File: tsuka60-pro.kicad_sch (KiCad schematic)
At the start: 173 parts, among them J1 USB_C_Receptacle_USB2.0, J2 Conn_01x04_MountingPin, SW1 SW_Reset, U1 ATmega32U4-M, U2 SRV05-4, Y1 16MHz

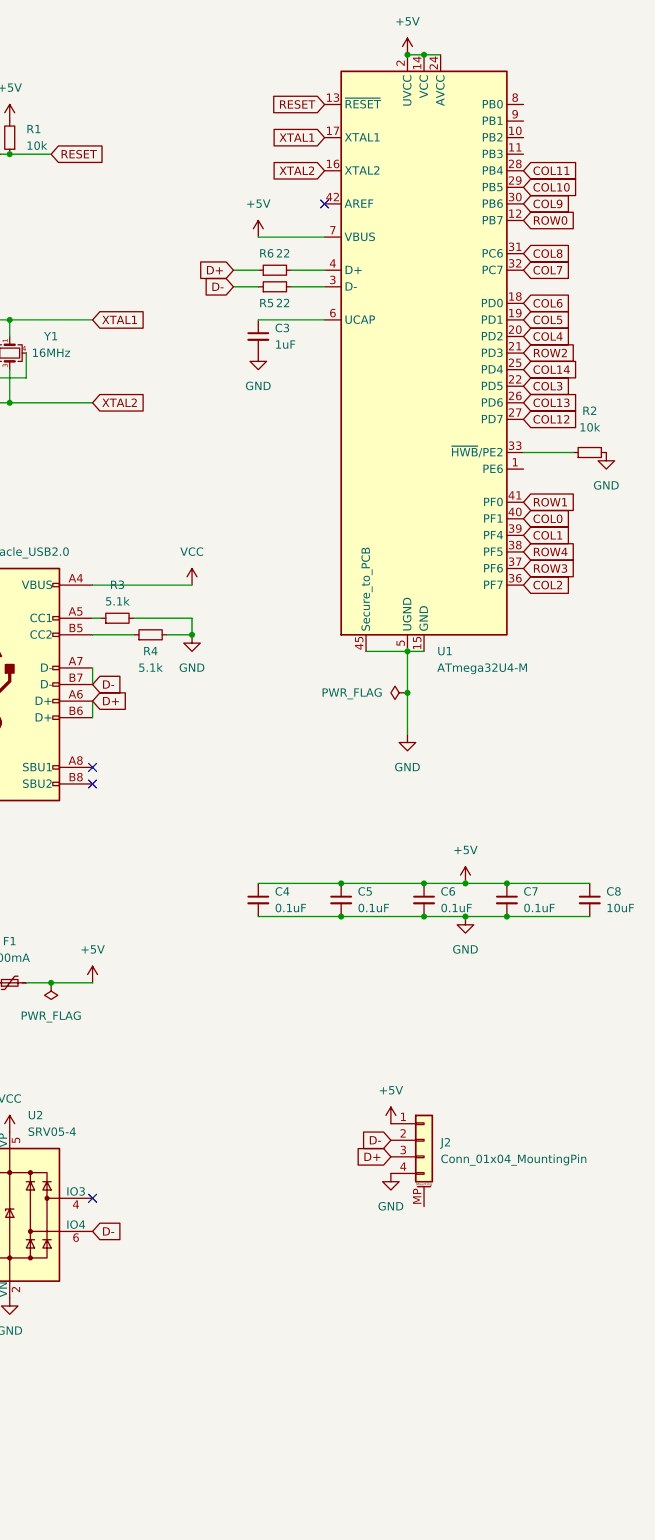
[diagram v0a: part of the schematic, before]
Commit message: SIP socket placement
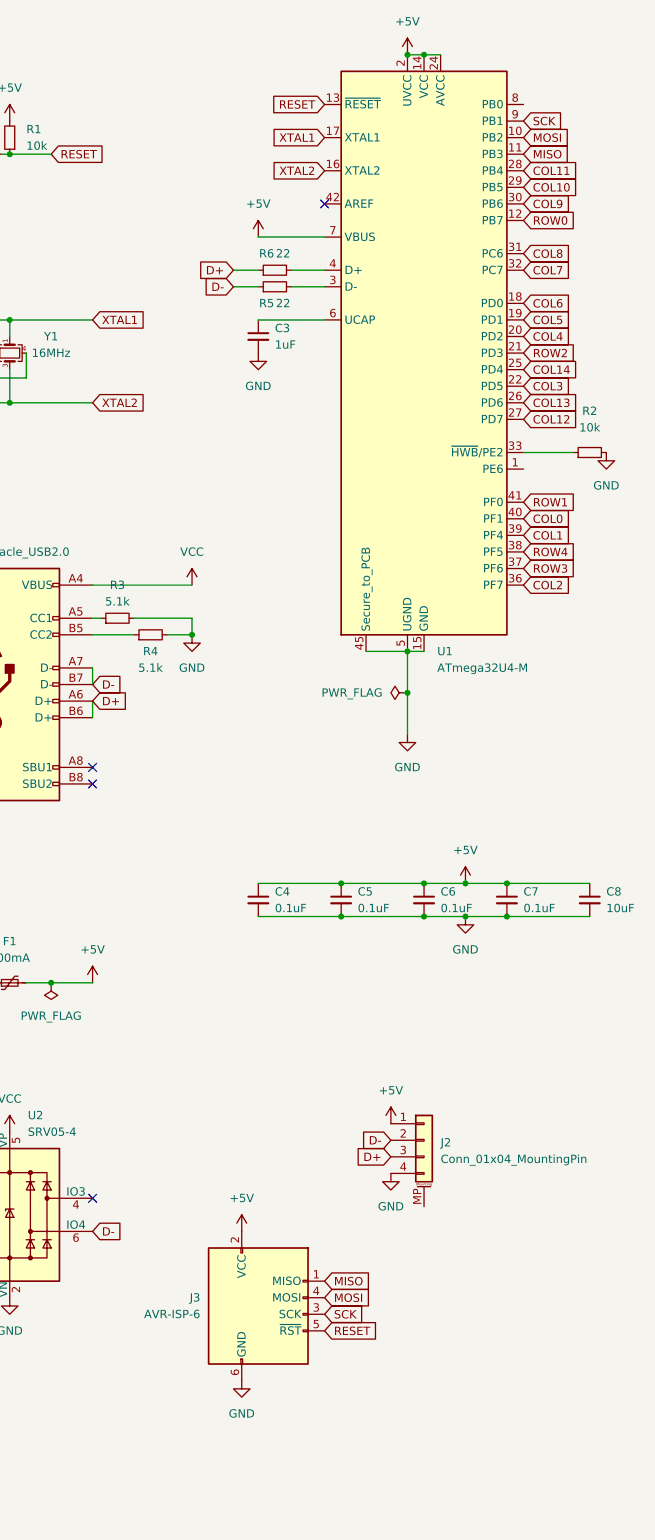
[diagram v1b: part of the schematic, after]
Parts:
- added J3: AVR-ISP-6, Connector_PinHeader_2.54mm:PinHeader_2x03_P2.54mm_Horizontal, symbol Connector:AVR-ISP-6
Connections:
- net +5V: now also J3.2 (VCC)
- net GND: now also J3.6 (GND)
- net RESET: now also J3.5 (~{RST})
- net MOSI: now reaches U1.10 (PB2)
- net MOSI: now also J3.4 (MOSI)
- net MISO: now reaches U1.11 (PB3)
- net MISO: now also J3.1 (MISO)
- net SCK: now reaches U1.9 (PB1)
- net SCK: now also J3.3 (SCK)
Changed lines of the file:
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@@
     )
   )
+  (global_label "SCK" (shape input) (at 340.36 228.6 0) (fields_autoplaced)
+    (effects (font (size 1.27 1.27)) (justify left))
+    (property "Intersheet References" "${INTERSHEET_REFS}" (id 0) (at 346.5226 228.5206 0)
+      (effects (font (size 1.27 1.27)) (justify left) hide)
+    )
+  )
   (global_label "COL14" (shape input) (at 234.95 38.1 180) (fields_autoplaced)
     (effects (font (size 1.27 1.27)) (justify right))
@@
     )
   )
+  (global_label "RESET" (shape input) (at 340.36 231.14 0) (fields_autoplaced)
+    (effects (font (size 1.27 1.27)) (justify left))
+    (property "Intersheet References" "${INTERSHEET_REFS}" (id 0) (at 348.5183 231.2194 0)
+      (effects (font (size 1.27 1.27)) (justify left) hide)
+    )
+  )
   (global_label "COL0" (shape input) (at 370.84 106.68 0) (fields_autoplaced)
     (effects (font (size 1.27 1.27)) (justify left))
@@
     )
   )
+  (global_label "SCK" (shape input) (at 370.84 45.72 0) (fields_autoplaced)
+    (effects (font (size 1.27 1.27)) (justify left))
+    (property "Intersheet References" "${INTERSHEET_REFS}" (id 0) (at 377.0026 45.6406 0)
+      (effects (font (size 1.27 1.27)) (justify left) hide)
+    )
+  )
   (global_label "COL12" (shape input) (at 209.55 38.1 180) (fields_autoplaced)
     (effects (font (size 1.27 1.27)) (justify right))
@@
     )
   )
+  (global_label "MOSI" (shape input) (at 340.36 226.06 0) (fields_autoplaced)
+    (effects (font (size 1.27 1.27)) (justify left))
+    (property "Intersheet References" "${INTERSHEET_REFS}" (id 0) (at 347.3693 225.9806 0)
+      (effects (font (size 1.27 1.27)) (justify left) hide)
+    )
+  )
   (global_label "ROW2" (shape input) (at 370.84 81.28 0) (fields_autoplaced)
     (effects (font (size 1.27 1.27)) (justify left))
@@
     )
   )
+  (global_label "MISO" (shape input) (at 370.84 50.8 0) (fields_autoplaced)
+    (effects (font (size 1.27 1.27)) (justify left))
+    (property "Intersheet References" "${INTERSHEET_REFS}" (id 0) (at 377.8493 50.7206 0)
+      (effects (font (size 1.27 1.27)) (justify left) hide)
+    )
+  )
   (global_label "D+" (shape input) (at 350.52 204.47 180) (fields_autoplaced)
     (effects (font (size 1.27 1.27)) (justify right))
@@
     )
   )
+  (global_label "MISO" (shape input) (at 340.36 223.52 0) (fields_autoplaced)
+    (effects (font (size 1.27 1.27)) (justify left))
+    (property "Intersheet References" "${INTERSHEET_REFS}" (id 0) (at 347.3693 223.4406 0)
+      (effects (font (size 1.27 1.27)) (justify left) hide)
+    )
+  )
   (global_label "ROW2" (shape input) (at 38.1 138.43 180) (fields_autoplaced)
     (effects (font (size 1.27 1.27)) (justify right))
@@
     )
   )
+  (global_label "MOSI" (shape input) (at 370.84 48.26 0) (fields_autoplaced)
+    (effects (font (size 1.27 1.27)) (justify left))
+    (property "Intersheet References" "${INTERSHEET_REFS}" (id 0) (at 377.8493 48.1806 0)
+      (effects (font (size 1.27 1.27)) (justify left) hide)
+    )
+  )
   (symbol (lib_id "Device:D_Small") (at 77.47 97.79 90) (unit 1)
     (in_bom yes) (on_board yes)
@@
     (pin "2")
   )
+  (symbol (lib_id "power:+5V") (at 327.66 215.9 0) (unit 1)
+    (in_bom yes) (on_board yes) (fields_autoplaced)
+    (property "Reference" "#PWR0101" (id 0) (at 327.66 219.71 0)
+      (effects (font (size 1.27 1.27)) hide)
+    )
+    (property "Value" "+5V" (id 1) (at 327.66 210.82 0))
+    (property "Footprint" "" (id 2) (at 327.66 215.9 0)
+      (effects (font (size 1.27 1.27)) hide)
+    )
+    (property "Datasheet" "" (id 3) (at 327.66 215.9 0)
+      (effects (font (size 1.27 1.27)) hide)
+    )
+    (pin "1")
+  )
   (symbol (lib_id "MX_Alps_Hybrid:MX-NoLED") (at 142.24 205.74 0) (unit 1)
     (in_bom yes) (on_board yes) (fields_autoplaced)
@@
     (pin "2")
   )
+  (symbol (lib_id "Connector:AVR-ISP-6") (at 330.2 228.6 0) (unit 1)
+    (in_bom yes) (on_board yes) (fields_autoplaced)
+    (property "Reference" "J3" (id 0) (at 321.31 226.0599 0)
+      (effects (font (size 1.27 1.27)) (justify right))
+    )
+    (property "Value" "AVR-ISP-6" (id 1) (at 321.31 228.5999 0)
+      (effects (font (size 1.27 1.27)) (justify right))
+    )
+    (property "Footprint" "Connector_PinHeader_2.54mm:PinHeader_2x03_P2.54mm_Horizontal" (id 2) (at 323.85 227.33 90)
+      (effects (font (size 1.27 1.27)) hide)
+    )
+    (property "Datasheet" " ~" (id 3) (at 297.815 242.57 0)
+      (effects (font (size 1.27 1.27)) hide)
+    )
+    (pin "1")
+    (pin "2")
+    (pin "3")
+    (pin "4")
+    (pin "5")
+    (pin "6")
+  )
   (symbol (lib_id "MX_Alps_Hybrid:MX-NoLED") (at 218.44 167.64 0) (unit 1)
     (in_bom yes) (on_board yes) (fields_autoplaced)
@@
     (pin "2")
   )
+  (symbol (lib_id "power:GND") (at 327.66 238.76 0) (unit 1)
+    (in_bom yes) (on_board yes) (fields_autoplaced)
+    (property "Reference" "#PWR0102" (id 0) (at 327.66 245.11 0)
+      (effects (font (size 1.27 1.27)) hide)
+    )
+    (property "Value" "GND" (id 1) (at 327.66 243.84 0))
+    (property "Footprint" "" (id 2) (at 327.66 238.76 0)
+      (effects (font (size 1.27 1.27)) hide)
+    )
+    (property "Datasheet" "" (id 3) (at 327.66 238.76 0)
+      (effects (font (size 1.27 1.27)) hide)
+    )
+    (pin "1")
+  )
   (symbol (lib_id "MX_Alps_Hybrid:MX-NoLED") (at 142.24 53.34 0) (unit 1)
     (in_bom yes) (on_board yes) (fields_autoplaced)
@@
       (reference "#PWR019") (unit 1) (value "GND") (footprint "")
     )
+    (path "/c1071c73-955d-4f63-9e9f-52f33f970f56"
+      (reference "#PWR0101") (unit 1) (value "+5V") (footprint "")
+    )
+    (path "/d64f4760-7922-472d-a587-dd43cd3c040f"
+      (reference "#PWR0102") (unit 1) (value "GND") (footprint "")
+    )
     (path "/0d4e228a-908e-4dad-a056-e4214b8aa2b1"
       (reference "C1") (unit 1) (value "22pF") (footprint "Capacitor_SMD:C_0603_1608Metric_Pad1.08x0.95mm_HandSolder")
@@
       (reference "J2") (unit 1) (value "Conn_01x04_MountingPin") (footprint "Connector_JST:JST_ACH_BM04B-ACHSS-A-GAN-ETF_1x04-1MP_P1.20mm_Vertical")
     )
+    (path "/cef45671-cd09-423e-8a15-fff58ac73c02"
+      (reference "J3") (unit 1) (value "AVR-ISP-6") (footprint "Connector_PinHeader_2.54mm:PinHeader_2x03_P2.54mm_Horizontal")
+    )
     (path "/bb3a180f-cdbc-49d0-97a9-6846eb214c84"

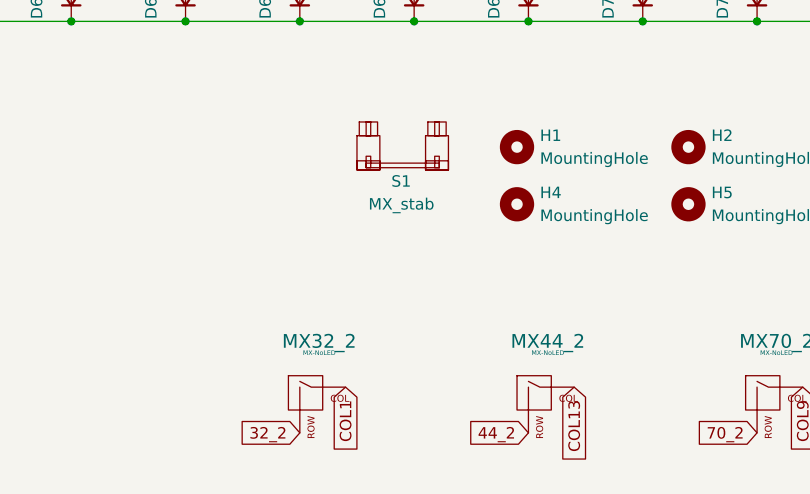
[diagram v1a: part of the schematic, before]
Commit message: Add 2u stab, relocate mounting holes
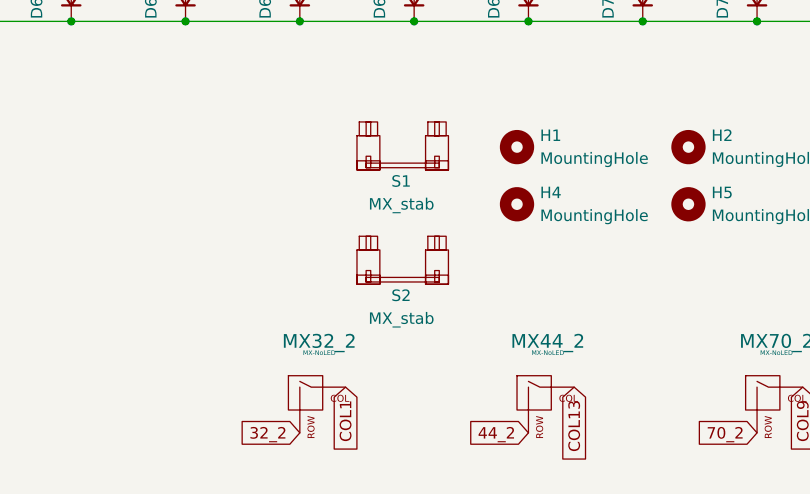
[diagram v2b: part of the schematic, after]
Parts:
- added S2: MX_stab, marbastlib-mx:STAB_MX_2u, symbol marbastlib-mx:MX_stab
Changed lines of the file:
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@@
     (pin "1")
+  )
+  (symbol (lib_id "marbastlib-mx:MX_stab") (at 139.7 241.3 0) (unit 1)
+    (in_bom yes) (on_board yes)
+    (property "Reference" "S2" (id 0) (at 138.43 245.11 0)
+      (effects (font (size 1.27 1.27)) (justify left))
+    )
+    (property "Value" "MX_stab" (id 1) (at 135.89 247.65 0)
+      (effects (font (size 1.27 1.27)) (justify left))
+    )
+    (property "Footprint" "marbastlib-mx:STAB_MX_2u" (id 2) (at 139.7 241.3 0)
+      (effects (font (size 1.27 1.27)) hide)
+    )
+    (property "Datasheet" "" (id 3) (at 139.7 241.3 0)
+      (effects (font (size 1.27 1.27)) hide)
+    )
   )
   (symbol (lib_id "Mechanical:MountingHole") (at 190.5 228.6 0) (unit 1)
@@
       (reference "S1") (unit 1) (value "MX_stab") (footprint "marbastlib-mx:STAB_MX_7u")
     )
+    (path "/47442934-60e8-4e6f-b94a-164ffe7747ad"
+      (reference "S2") (unit 1) (value "MX_stab") (footprint "marbastlib-mx:STAB_MX_2u")
+    )
     (path "/8177a6bd-bc14-4714-bc96-ad252ffed026"

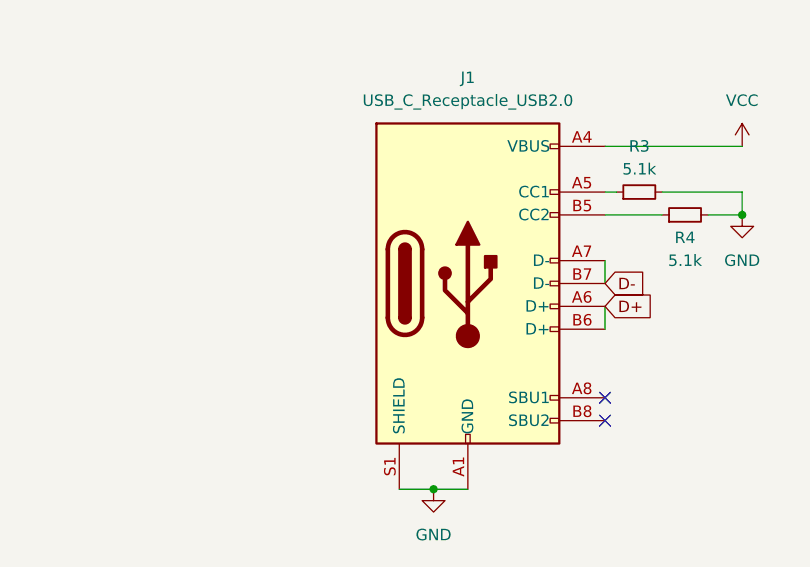
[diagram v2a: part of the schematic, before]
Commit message: Update traces and BOM, production files
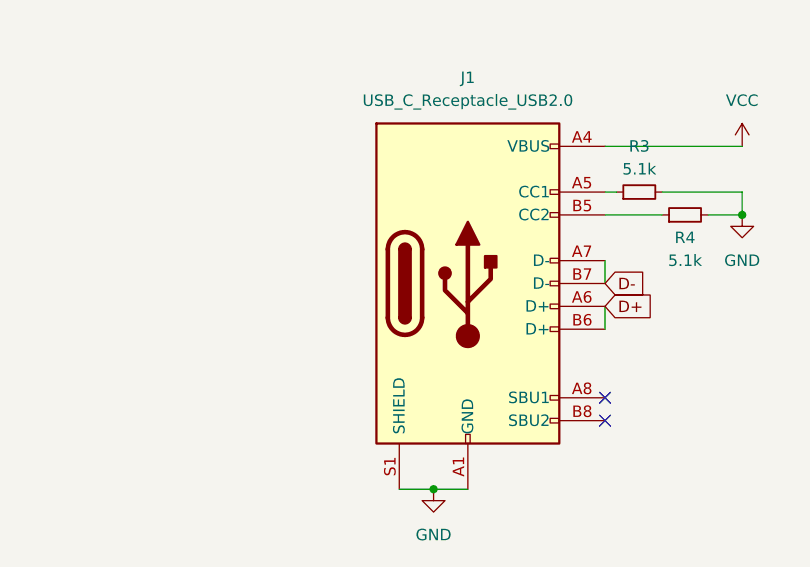
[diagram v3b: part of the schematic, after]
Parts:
- H1, H2, H3, H4, H5, H6: footprint MountingHole:MountingHole_2.2mm_M2_Pad_TopOnly -> MountingHole:MountingHole_2.5mm

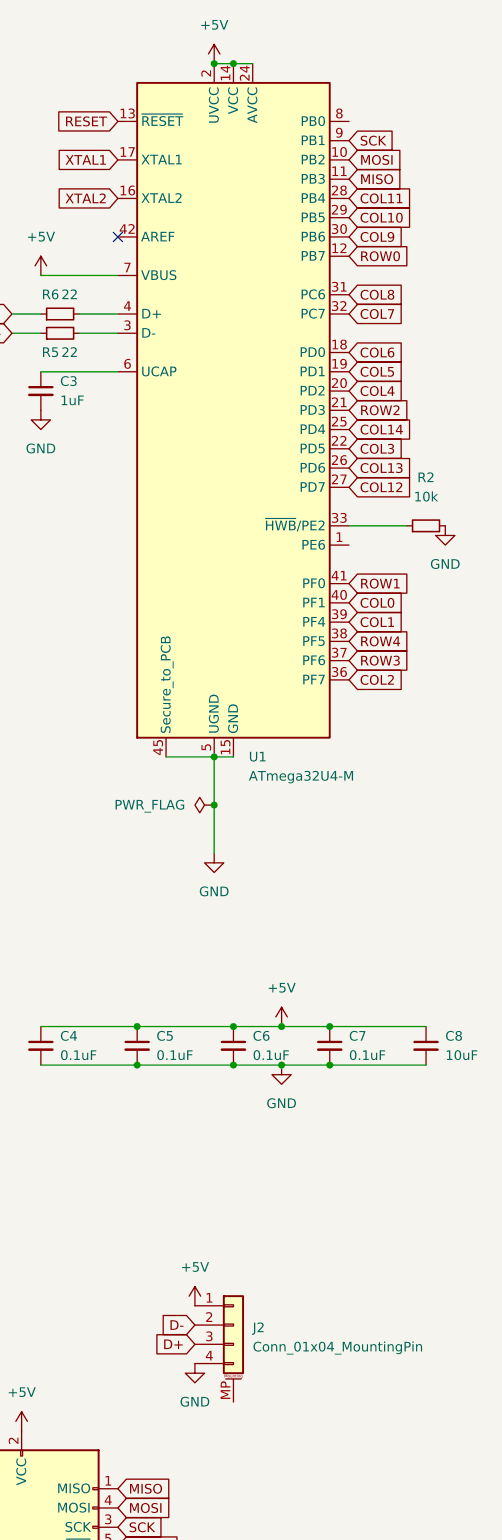
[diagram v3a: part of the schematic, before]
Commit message: Fixed some ERC and DRC errors
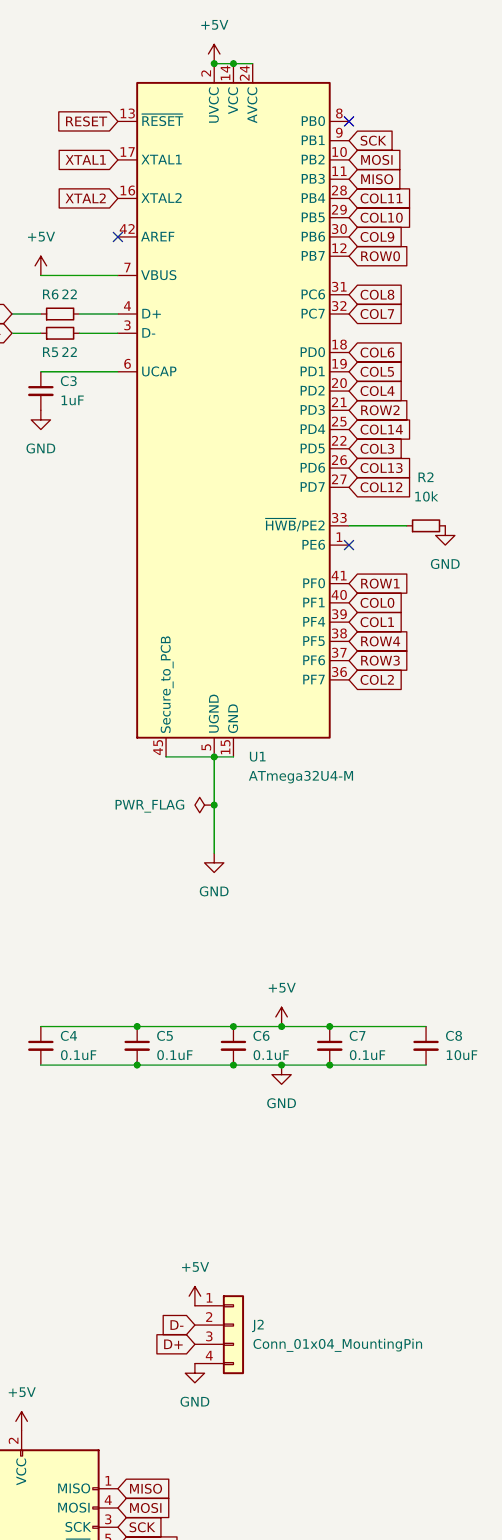
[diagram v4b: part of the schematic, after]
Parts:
- J2: symbol Connector_Generic_MountingPin:Conn_01x04_MountingPin -> Connector_Generic:Conn_01x04
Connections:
- no-connect marks 5 -> 7
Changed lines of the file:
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@@
 	)
 	(no_connect
+		(at 370.84 99.06)
+	)
+	(no_connect
 		(at 340.36 58.42)
 	)
@@
 	)
 	(no_connect
+		(at 370.84 43.18)
+	)
+	(no_connect
 		(at 304.8 210.82)
 	)
@@
 	)
 	(symbol
-		(lib_id "Connector_Generic_MountingPin:Conn_01x04_MountingPin")
+		(lib_id "Connector_Generic:Conn_01x04")
 		(at 355.6 201.93 0)
 		(unit 1)
@@
 		(fields_autoplaced yes)
 		(property "Reference" "J2"
-			(at 358.14 202.2855 0)
+			(at 358.14 201.9299 0)
 			(effects
 				(font
@@
 		)
 		(property "Value" "Conn_01x04_MountingPin"
-			(at 358.14 204.8255 0)
+			(at 358.14 204.4699 0)
 			(effects
 				(font
@@
 			)
 		)
-		(property "Description" ""
+		(property "Description" "Generic connector, single row, 01x04, script generated (kicad-library-utils/schlib/autogen/connector/)"
 			(at 355.6 201.93 0)
 			(effects
@@
 					(size 1.27 1.27)
 				)
+				(hide yes)
 			)
 		)
@@
 		(pin "4"
 		)
-		(pin "MP"
-		)
 		(instances
